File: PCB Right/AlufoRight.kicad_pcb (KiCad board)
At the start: 2 copper layers, 282.6 x 90.9 mm, 94 parts, among them J10 Shield_Connection, J2 USB_C_Receptacle_USB2.0_16P_2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, J4 USB_C_Receptacle_USB2.0_16P_2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, J6 Shield_Connection, J8 Shield_Connection, K11 PG1350, K12 PG1350, K13 PG1350, K14 PG1350, K15 PG1350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

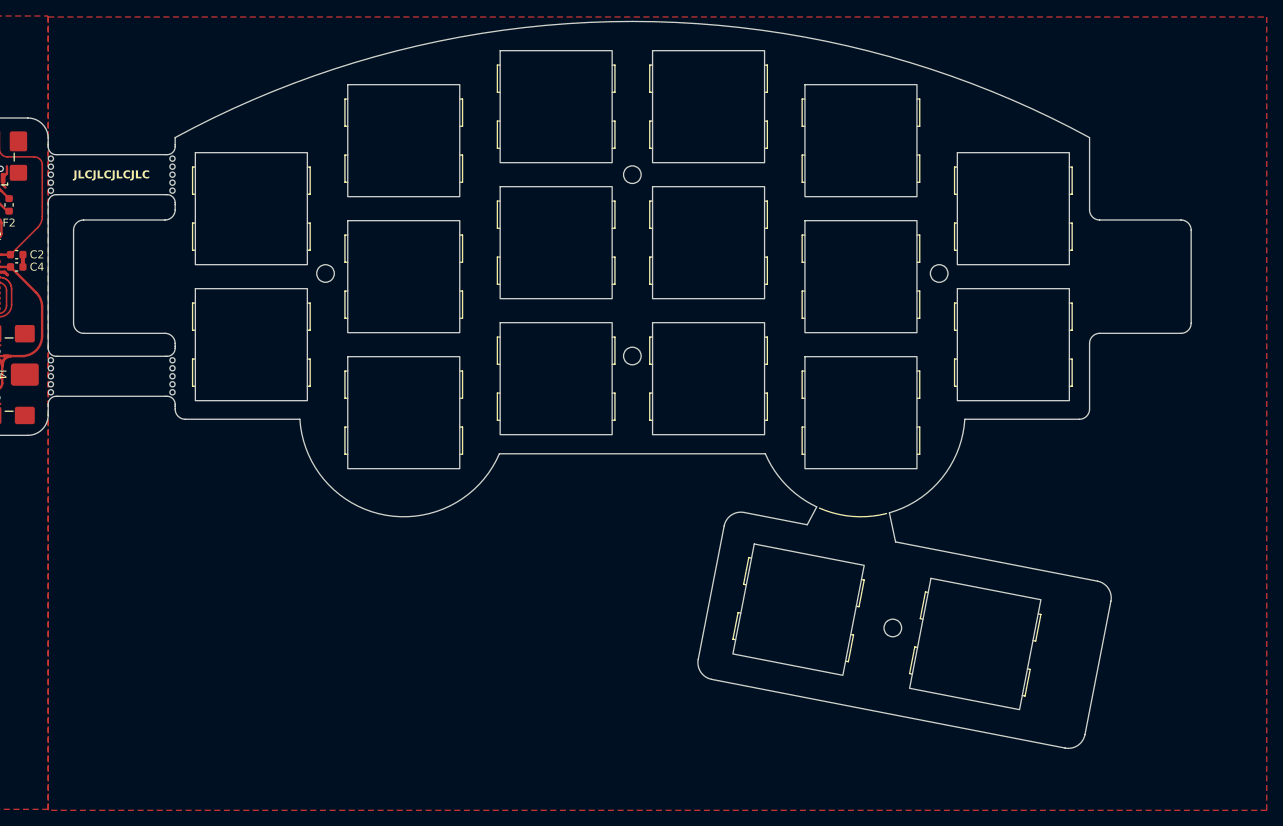
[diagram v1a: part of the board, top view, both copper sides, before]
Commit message: Remove plate from left and right PCBs
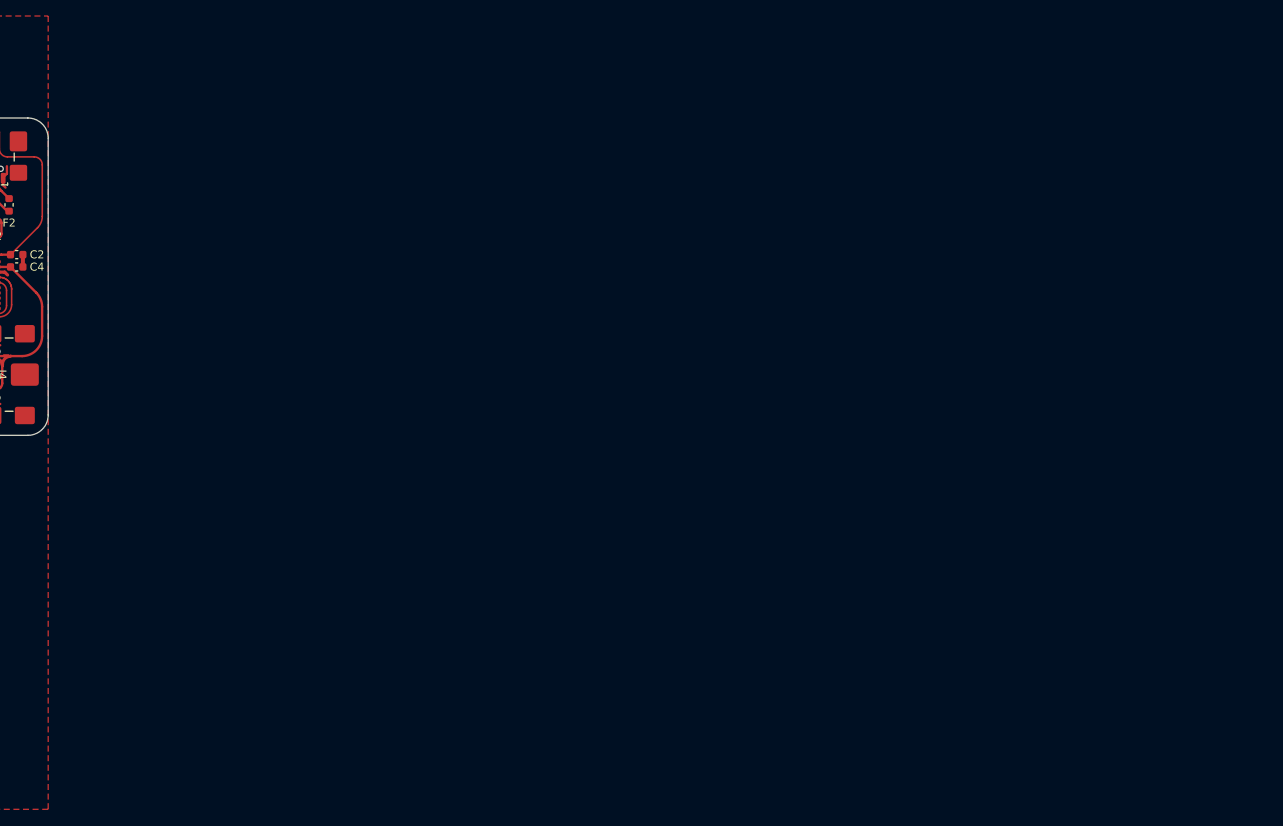
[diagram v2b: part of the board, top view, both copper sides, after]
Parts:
- removed H10, H6, H7, H8, H9: ScrewHole, MountingHole:MountingHole_2.2mm_M2
- removed H11, H12, H13, H14: Mousebites, Project_Library:Mousebites
- removed PK11, PK12, PK13, PK14, PK15, PK16, PK21, PK22, PK23, PK24, PK25, PK26, PK32, PK33, PK34, PK35, PK42: SwitchHole, Project_Library:SW_choc_v1_Plate_CPG135001S30_1u
- removed PK41: SwitchHole, Project_Library:SW_choc_v1_Plate_CPG135001S30_1.5u
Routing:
- removed copper zone on F.Cu, net (none)
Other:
- board size 282.6 x 90.9 mm -> 139.7 x 90.9 mm
- board text removed: "JLCJLCJLCJLC"
